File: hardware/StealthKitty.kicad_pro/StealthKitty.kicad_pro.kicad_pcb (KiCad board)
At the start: 4 copper layers, 53.9 x 57 mm, 77 parts, among them IC501 MP1475DJ-LF-P, J201 Conn_01x06, J202 Conn_01x06, J302 Conn_01x06, SW501 Switch, U301 ADXL343, U401 STM32G431CBU6

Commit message: Modif PCB 16/10/2024 V2
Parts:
- removed MISO: TestPoint, TestPoint:TestPoint_Pad_D1.5mm
- added D403: LED_status_LiDAR, LED_SMD:LED_0603_1608Metric_Pad1.05x0.95mm_HandSolder, F.Cu at (145.7, 107.7)
- added R405: 1k, Resistor_SMD:R_0402_1005Metric, F.Cu at (147.0, 108.1)
- added TP307: TestPoint, TestPoint:TestPoint_Pad_D1.5mm, F.Cu at (158.3, 94.6)
- C201, C202, C203, C206, C207, C208, C402, C407, C410, C504, C506, Cs301: footprint Capacitor_SMD:C_0402_1005Metric -> Capacitor_SMD:C_0603_1608Metric
- C501, C507, C509: footprint Capacitor_SMD:C_0402_1005Metric -> Capacitor_SMD:C_0805_2012Metric
- SW401: renamed from NRST SW
- TP201: renamed from PWM1 CH1
- TP202: renamed from PWM1 CH2
- TP203: renamed from PWM2 CH1
- TP204: renamed from PWM2 CH2
- U1: renamed from Driver 1
- U2: renamed from Driver 2
- moved TP310 22.2 mm to (166.0, 85.3)
- moved TP302 20.2 mm to (166.0, 82.6)
- moved TP309 17.4 mm to (164.4, 94.9)
- moved TP308 3.61 mm to (163.9, 90.9)
- moved TP203 3.48 mm to (144.1, 105.0)
- moved C407 2.57 mm to (147.4, 95.0), turned to 0 degrees
- moved C507 1.56 mm to (158.1, 89.9), turned to -90 degrees
- moved C509 1.47 mm to (160.3, 89.9), turned to -90 degrees
- moved C503 1.39 mm to (154.0, 88.2), turned to -90 degrees
- moved TP204 1.36 mm to (143.7, 102.0)
- moved C501 1.31 mm to (155.6, 89.0), turned to -90 degrees
- moved C203 1.31 mm to (137.6, 89.4)
- moved L501 1.30 mm to (161.7, 84.6)
- moved C204 1.30 mm to (136.8, 86.6), turned to 90 degrees
- moved C505 1.29 mm to (157.7, 81.9)
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- renumbered Alim_charger to Alim_charger501, Status_Orange to D401, Status_Purple to D402, TOF2 to J301, LIDAR to J303, STLink to J401, Button_1 to SW402, SCK to TP301, nCS to TP302, MOSI to TP308, INT2 to TP309, INT1 to TP310, Quartz to Y401
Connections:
- U401 pad 38: unconnected-(U401-PA15-Pad38) -> /brain Sheet/status_LiDAR
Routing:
- net INT2_adx: track 12.8 -> 21.7 mm, vias 2 -> 4
- net nCS: track 20.7 -> 13.8 mm
- net /brain Sheet/status_LiDAR: track 0.00 -> 6.47 mm, vias 0 -> 2
- net GND: track 41.1 -> 47.1 mm
- net INT1_adx: track 16.0 -> 10.8 mm
- net +VBAT: track 8.82 -> 11.8 mm, vias 7 -> 11
- net SCK: track 14.8 -> 17.6 mm
- net MISO: track 10.8 -> 13.5 mm
- net +5V: track 85.4 -> 87.9 mm, vias 6 -> 7
- net MOSI: track 17.2 -> 19.5 mm, vias 3 -> 4
- net Net-(BT501-+): track 11.9 -> 13.4 mm
- net Rx_lidar: track 34.3 -> 35.8 mm
- net Net-(D403-K): track 0.00 -> 1.32 mm
- net PWM_MOT1_CH2: track 25.7 -> 24.6 mm
- net PWM_MOT2_CH2: track 10.4 -> 9.32 mm
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- added copper zone on F.Cu, net Net-(IC501-SW)

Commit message: Modif PCB 17/10/2024 V3
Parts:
- moved TP310 1.50 mm to (165.9, 86.8)
- moved Cs301 0.62 mm to (147.5, 89.1)
- moved C407 0.40 mm to (147.4, 95.4)
- moved TP302 0.10 mm to (165.9, 82.6)
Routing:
- net INT1_adx: track 10.8 -> 29.9 mm, vias 2 -> 4
- net nCS: track 13.8 -> 31.3 mm, vias 3 -> 4
- net +3.3V: track 22.2 -> 23.4 mm
- net GND: track 47.1 -> 46.4 mm
- net INT2_adx: track 21.7 -> 21.1 mm

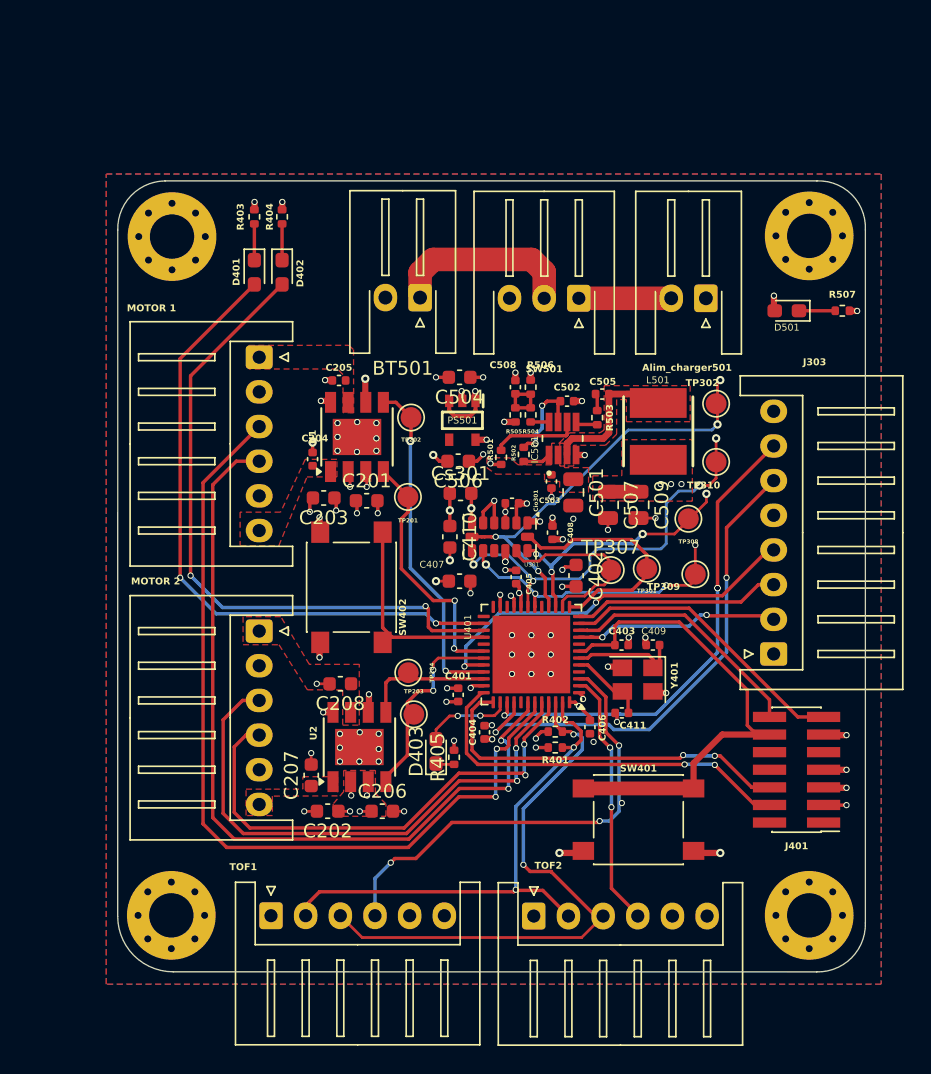
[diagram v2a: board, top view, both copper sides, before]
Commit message: Routage final pour vérification prof
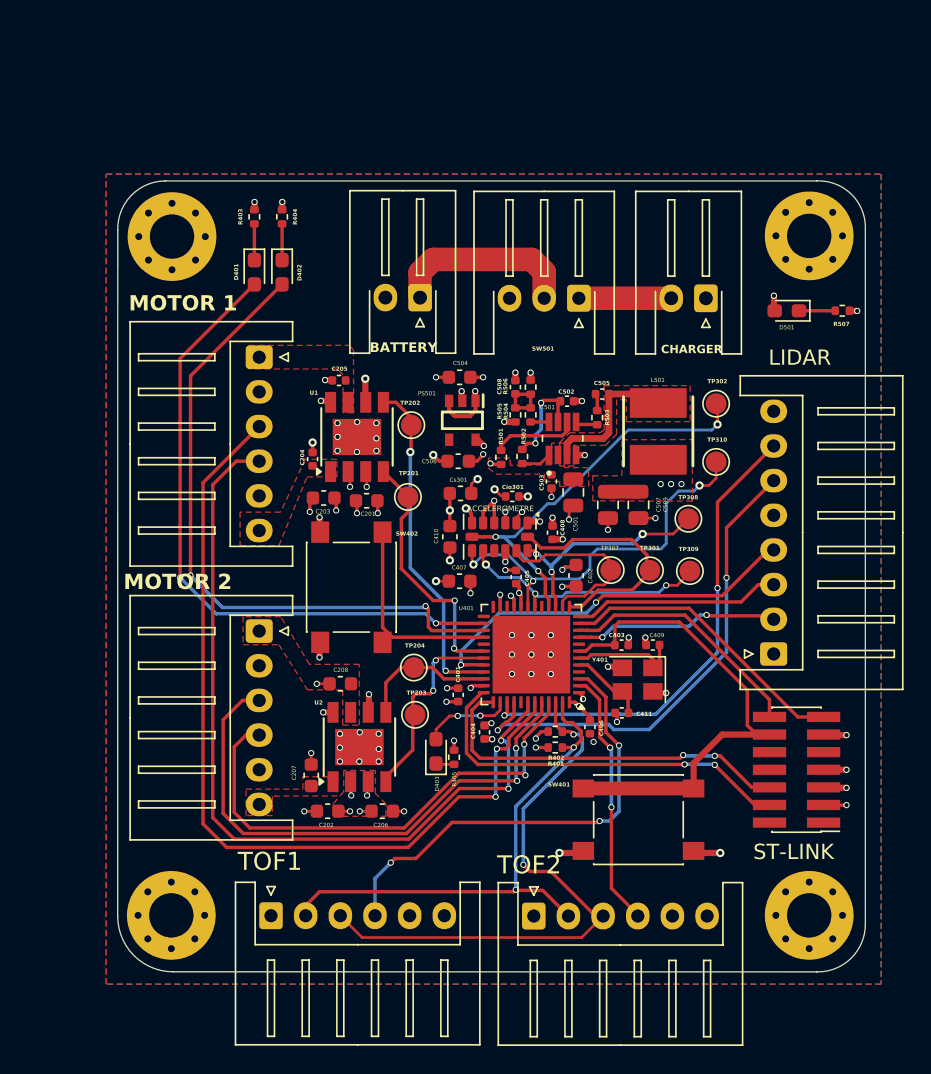
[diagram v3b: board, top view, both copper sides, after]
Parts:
- moved TP202 0.55 mm to (143.9, 84.2)
- moved TP204 0.54 mm to (144.1, 101.6)
- moved Cio301 0.49 mm to (151.2, 89.3)
- moved TP309 0.45 mm to (164.0, 94.7)
- moved TP301 0.26 mm to (161.1, 94.6)
- moved R502 0.18 mm to (151.9, 86.4)
- moved TP203 0.10 mm to (144.2, 105.0)
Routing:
- net MOSI: track 19.5 -> 17.1 mm, vias 4 -> 3
- net INT2_adx: track 21.1 -> 19.2 mm, vias 4 -> 3
- net nCS: track 31.3 -> 29.6 mm, vias 4 -> 3
- net INT1_adx: track 29.9 -> 28.2 mm, vias 4 -> 3
- net GND: track 46.4 -> 47.4 mm, vias 74 -> 73
- net +3.3V: track 23.4 -> 24.1 mm, vias 21 -> 23
- net PWM_MOT2_CH2: track 9.32 -> 9.99 mm
- net Tx_Lidar: vias 3 -> 2
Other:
- board text added: "ACCELEROMETRE"
- board text added: "BATTERY"
- board text added: "CHARGER"
- board text added: "LIDAR"
- board text added: "ST-LINK"

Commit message: MODIF PCB 22/10/2024
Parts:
- removed C410: 1u, Capacitor_SMD:C_0603_1608Metric
- added C412: 100nF, Capacitor_SMD:C_0402_1005Metric, F.Cu at (137.4, 101.5)
- added R406: 10k, Resistor_SMD:R_0402_1005Metric, F.Cu at (141.3, 102.0)
- added R407: 10K, Resistor_SMD:R_0402_1005Metric, F.Cu at (139.4, 101.5)
- moved TP302 21.7 mm to (146.2, 91.7)
- moved C408 5.12 mm to (150.1, 95.1), turned to -90 degrees
- moved C202 1.53 mm to (139.2, 112.8), turned to -90 degrees
- moved C206 1.34 mm to (140.7, 112.8), turned to -90 degrees
- moved C208 0.95 mm to (137.9, 103.0)
- moved C411 0.62 mm to (159.7, 104.8), turned to 0 degrees
- moved C407 0.57 mm to (147.8, 95.8)
- moved C401 0.56 mm to (147.2, 103.0), turned to 180 degrees
- moved Cs301 0.19 mm to (147.6, 88.9)
- moved C506 0.16 mm to (147.4, 86.8)
- moved Cio301 0.14 mm to (151.2, 89.2)
- moved TP309 0.06 mm to (163.9, 94.7)
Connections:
- SW402 pad 1: /brain Sheet/Button_1 -> Net-(R406-Pad2)
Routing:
- net +5V: track 87.9 -> 8.57 mm
- net Net-(R406-Pad2): track 0.00 -> 14.6 mm, vias 0 -> 2
- net +3.3V: track 24.1 -> 38.0 mm, vias 23 -> 17
- net nCS: track 29.6 -> 18.5 mm, vias 3 -> 2
- net Codeur2_PH1: track 39.8 -> 41.9 mm
- net Codeur1_PH2: track 62.0 -> 64.1 mm
- net Codeur2_PH2: track 36.1 -> 38.1 mm
- net GND: track 47.4 -> 46.1 mm, vias 73 -> 82
- net Codeur1_PH1: track 59.0 -> 60.2 mm
- net Rx_lidar: track 35.5 -> 34.3 mm
- net /brain Sheet/Button_1: track 14.6 -> 13.7 mm
- net /brain Sheet/status_Purple: track 47.4 -> 46.6 mm
- net +VBAT: track 11.8 -> 12.5 mm, vias 11 -> 9
- net /brain Sheet/OSC_IN: track 5.65 -> 6.23 mm
- net Tx_Lidar: track 34.8 -> 35.4 mm
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
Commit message: Modif après revue du prof le 22/10
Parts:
- moved C407 0.53 mm to (147.4, 95.6), turned to 180 degrees
- moved Cio301 0.24 mm to (151.2, 88.9)
- moved C502 0.10 mm to (155.1, 82.3)
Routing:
- net +3.3V: track 38.0 -> 47.7 mm
- net GND: track 46.1 -> 47.0 mm, vias 82 -> 95
- net PWM_MOT1_CH1: track 18.4 -> 17.6 mm
- net M_SCTR: track 28.3 -> 29.0 mm
- net Rx_lidar: track 34.3 -> 34.9 mm

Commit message: Ajout fichier GERBER
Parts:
- added G***: LOGO, Library:LOGO, F.Cu at (146.5, 113.5)
- H403: moved to B.Cu
- turned H403 to 180 degrees
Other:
- board text added: "StealthKitty"

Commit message: Ajout fichier GERBER zip
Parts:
- moved C206 12.0 mm to (135.1, 102.2)
- moved C509 12.0 mm to (154.6, 79.3)
- moved Cs301 12.0 mm to (141.9, 78.3)
- moved J302 12.0 mm to (128.1, 109.0)
- moved J303 12.0 mm to (164.4, 90.1)
- moved R401 12.0 mm to (148.6, 96.8)
- moved BT501 12.0 mm to (138.9, 64.4)
- moved C204 12.0 mm to (131.1, 76.0)
- moved C402 12.0 mm to (150.1, 84.5)
- moved C406 12.0 mm to (151.1, 95.4)
- moved C508 12.0 mm to (145.8, 70.9)
- moved H402 12.0 mm to (166.9, 60.0)
- moved H403 12.0 mm to (166.9, 109.0)
- moved R402 12.0 mm to (148.6, 95.7)
- moved R406 12.0 mm to (135.6, 91.4)
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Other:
- board size 53.9 x 57 mm -> 54 x 57 mm

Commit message: Ajout fichier GERBER final
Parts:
- moved H402 0.07 mm to (167.0, 60.0)
- moved H403 0.07 mm to (167.0, 109.0)
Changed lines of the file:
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@@
 	(footprint "MountingHole:MountingHole_3.2mm_M3_Pad_Via"
 		(layer "F.Cu")
-		(at 166.95 59.95)
+		(at 167 60)
 		(descr "Mounting Hole 3.2mm, M3")
 		(tags "mounting hole 3.2mm m3")
@@
 	(footprint "MountingHole:MountingHole_3.2mm_M3_Pad_Via"
 		(layer "F.Cu")
-		(at 120.95 108.95)
+		(at 121 108.95)
 		(descr "Mounting Hole 3.2mm, M3")
 		(tags "mounting hole 3.2mm m3")
@@
 	(footprint "MountingHole:MountingHole_3.2mm_M3_Pad_Via"
 		(layer "B.Cu")
-		(at 166.95 108.95 180)
+		(at 167 109 180)
 		(descr "Mounting Hole 3.2mm, M3")
 		(tags "mounting hole 3.2mm m3")
